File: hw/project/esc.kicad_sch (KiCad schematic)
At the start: 0 parts

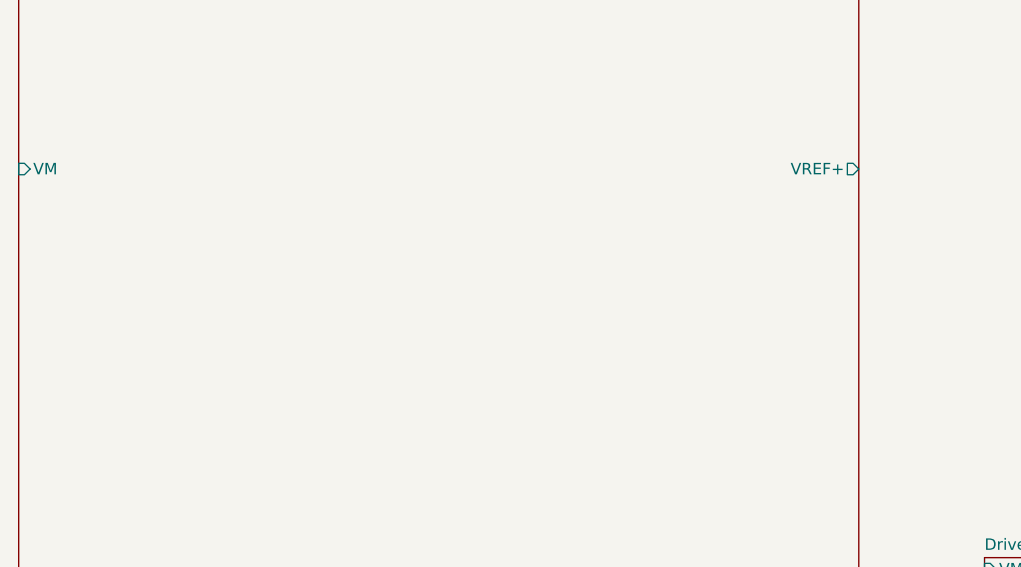
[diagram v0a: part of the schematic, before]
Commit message: Create new hierarchical pins for OPAMPx
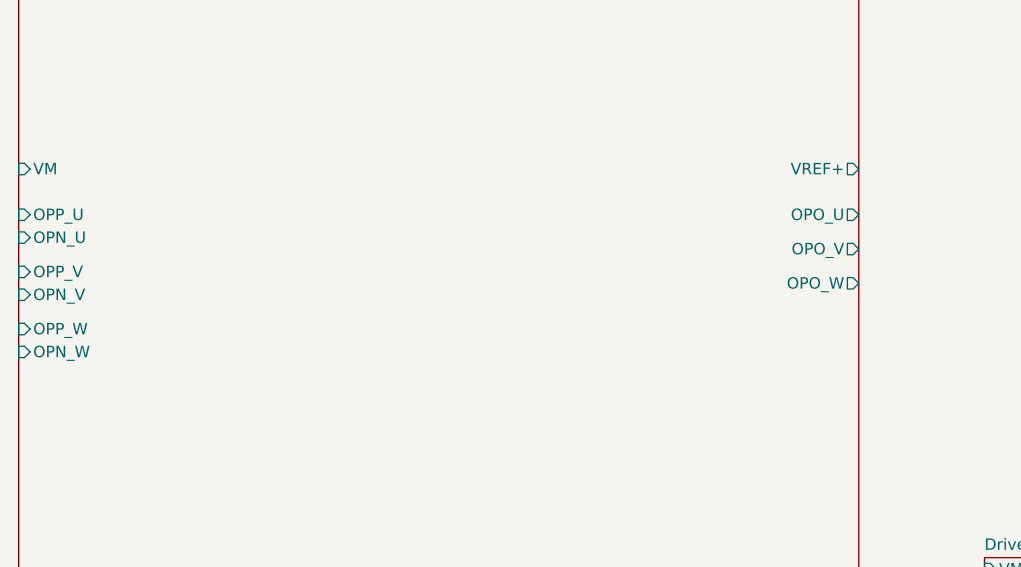
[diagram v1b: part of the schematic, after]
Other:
- sheet Control ports: added OPN_U, OPN_V, OPN_W, OPO_U, OPO_V, OPO_W, OPP_U, OPP_V, OPP_W; removed none
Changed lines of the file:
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@@
+			)
+		)
+		(pin "OPN_U" input
+			(at 13.335 46.99 180)
+			(effects
+				(font
+					(size 1.27 1.27)
+				)
+				(justify left)
+			)
+		)
+		(pin "OPN_V" input
+			(at 13.335 53.34 180)
+			(effects
+				(font
+					(size 1.27 1.27)
+				)
+				(justify left)
+			)
+		)
+		(pin "OPN_W" input
+			(at 13.335 59.69 180)
+			(effects
+				(font
+					(size 1.27 1.27)
+				)
+				(justify left)
+			)
+		)
+		(pin "OPO_U" output
+			(at 106.68 44.45 0)
+			(effects
+				(font
+					(size 1.27 1.27)
+				)
+				(justify right)
+			)
+		)
+		(pin "OPO_V" output
+			(at 106.68 48.26 0)
+			(effects
+				(font
+					(size 1.27 1.27)
+				)
+				(justify right)
+			)
+		)
+		(pin "OPO_W" output
+			(at 106.68 52.07 0)
+			(effects
+				(font
+					(size 1.27 1.27)
+				)
+				(justify right)
+			)
+		)
+		(pin "OPP_U" input
+			(at 13.335 44.45 180)
+			(effects
+				(font
+					(size 1.27 1.27)
+				)
+				(justify left)
+			)
+		)
+		(pin "OPP_V" input
+			(at 13.335 50.8 180)
+			(effects
+				(font
+					(size 1.27 1.27)
+				)
+				(justify left)
+			)
+		)
+		(pin "OPP_W" input
+			(at 13.335 57.15 180)
+			(effects
+				(font
+					(size 1.27 1.27)
+				)
+				(justify left)
 			)
 		)
